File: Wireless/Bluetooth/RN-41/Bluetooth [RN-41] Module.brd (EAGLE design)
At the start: 25.4 x 25.4 mm, 12 parts

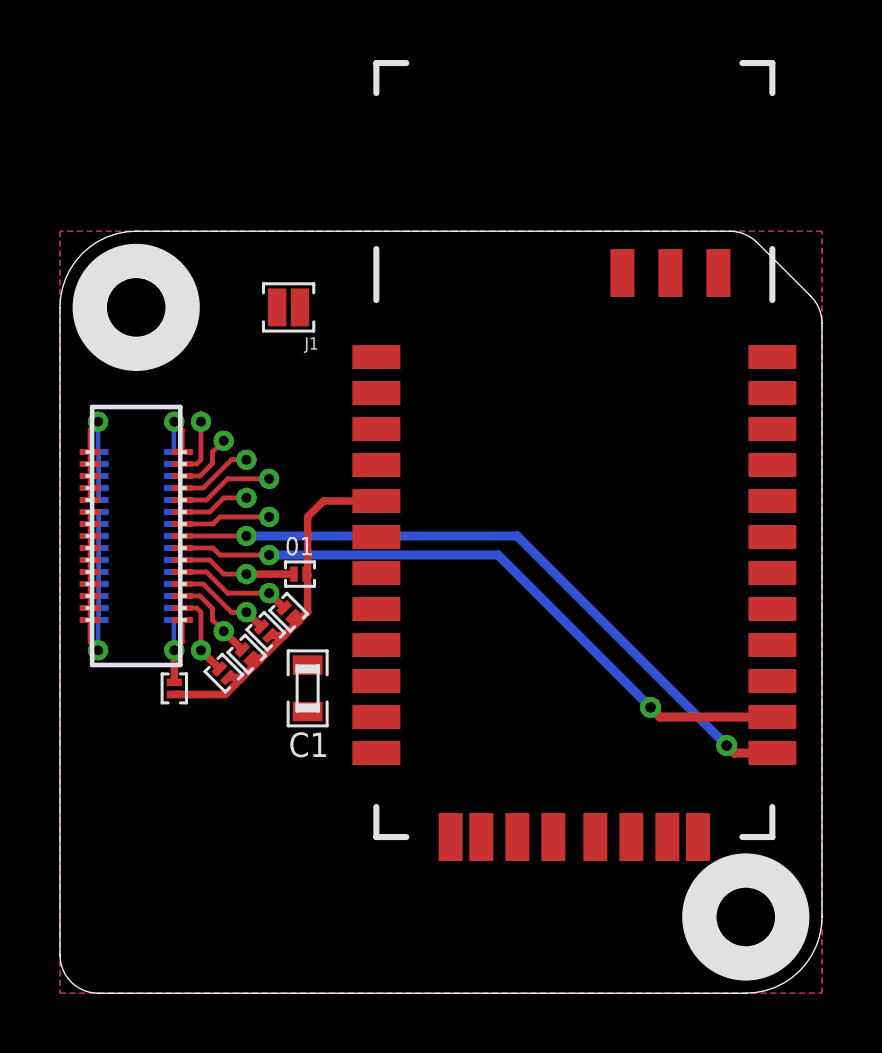
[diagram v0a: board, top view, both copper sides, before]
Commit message: Completed Bluetooth (RN-41) Module
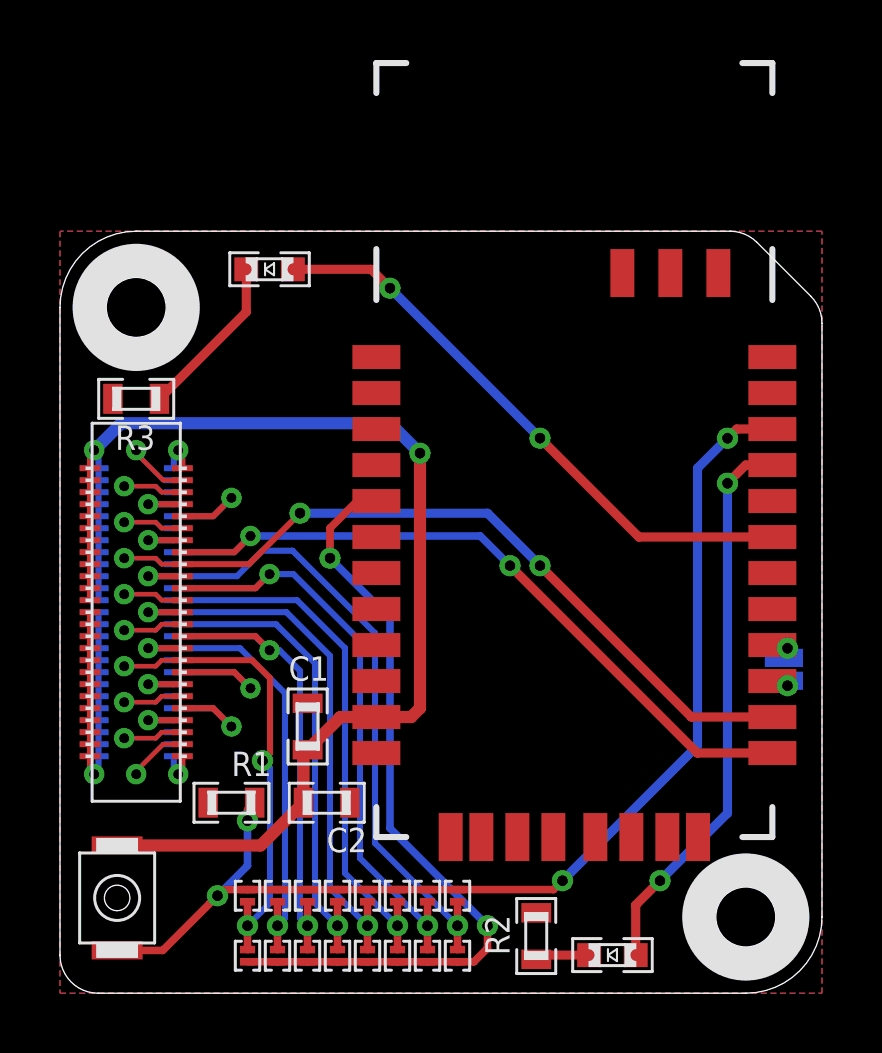
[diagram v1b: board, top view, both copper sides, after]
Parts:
- removed 02, 03: (no value), .solderjumper:2.SML
- added 08, J10, J11, J12, J13, J14, J15, J2, J3, J4, J8, J9: (no value), .solderjumper:2.SML
- added BTN1: SPST.B3U-1000P(M)-B, omron:B3U-1000P(M)-B
- added C2: 1uF, .standardparts:0603
- added LED1, LED2: (no value), .standardparts:0603.LED
- added R1: 100k, .standardparts:0603
- added R2, R3: 1k, .standardparts:0603
- C1: value (none) -> .1uF
- moved J1 20.4 mm to (24.1, 10.8), flipped to the bottom, turned to 270 degrees
- moved J5 11.2 mm to (11.2, 1.25), turned to 270 degrees
- moved 01 10.9 mm to (6.25, 3.25), turned to 90 degrees
- moved J6 10.6 mm to (10.2, 1.25), turned to 270 degrees
- moved J7 10.4 mm to (9.25, 1.25)
- moved C1 1.27 mm to (8.26, 8.89)
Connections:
- new net 01: J2.1, J4.1, U$8.01, U$8.01@1, U$8.01@VIA
- new net 02: J10.1, J3.1, U$8.02, U$8.02@1, U$8.02@VIA
- new net 03: J11.1, J5.1, U$8.03, U$8.03@1, U$8.03@VIA
- new net 04: J12.1, J6.1, U$8.04, U$8.04@1, U$8.04@VIA
- new net 05: J13.1, J7.1, U$8.05, U$8.05@1, U$8.05@VIA
- new net 06: J14.1, J8.1, U$8.06, U$8.06@1, U$8.06@VIA
- new net 07: J15.1, J9.1, U$8.07, U$8.07@1, U$8.07@VIA
- new net N$16: U$8.RXI.DBG, U$8.RXI.DBG@1, U$8.RXI.DBG@VIA
- new net N$17: U$8.TXO.DBG, U$8.TXO.DBG@1, U$8.TXO.DBG@VIA
- new net N$19: U$8.RST, U$8.RST@1, U$8.RST@VIA
- new net N$23: LED1.P$2, R3.1
- new net WAKE: 01.1, 08.1, U$8.WAKE, U$8.WAKE@1, U$8.WAKE@VIA
- net 3.3V: now also BTN1.2, C2.1, U$8.3.3V@11, U$8.3.3V@12, U$8.3.3V@13, U$8.3.3V@14, U$8.3.3V@15, U$8.3.3V@16, U$8.3.3V@17, U$8.3.3V@18, U$8.3.3V@19, U$8.3.3V@20, U$8.3.3V@21, U$8.3.3V@22, U$8.3.3V@23, U$8.3.3V@24
- net AUTO.DISC: now also U$2.20; no longer U$2.22
- net CONNECTED: now also LED1.P$1
- net FACTORY.RST: now also 01.2, BTN1.1, J10.2, J11.2, J12.2, J13.2, J14.2, J15.2, J4.2, R1.1, U$2.22; no longer U$2.20
- net GND: now also C2.2, R1.2, R2.2, R3.2, U$8.GND@21, U$8.GND@22, U$8.GND@23, U$8.GND@24, U$8.GND@25, U$8.GND@26
- net N$10: now also LED2.P$2, R2.1; no longer 01.1, U$8.03, U$8.03@1, U$8.03@VIA
- net N$11: now also U$8.TRST, U$8.TRST@1, U$8.TRST@VIA; no longer 02.1, U$8.04, U$8.04@1, U$8.04@VIA
- net N$12: now also U$8.TMS, U$8.TMS@1, U$8.TMS@VIA; no longer 03.1, U$8.05, U$8.05@1, U$8.05@VIA
- net N$13: now also U$8.TCK, U$8.TCK@1, U$8.TCK@VIA; no longer J5.1, U$8.06, U$8.06@1, U$8.06@VIA
- net N$14: now also U$8.TDO, U$8.TDO@1, U$8.TDO@VIA; no longer J6.1, U$8.07, U$8.07@1, U$8.07@VIA
- net N$15: now also U$8.TDI, U$8.TDI@1, U$8.TDI@VIA; no longer J7.1, U$8.WAKE, U$8.WAKE@1, U$8.WAKE@VIA
- net RST: now also 08.2, J2.2, J3.2, J8.2, J9.2; no longer 01.2, 02.2, 03.2
- net RXI: now also U$8.RXI, U$8.RXI@1, U$8.RXI@VIA; no longer U$8.02, U$8.02@1, U$8.02@VIA
- net STATUS: now also LED2.P$1
- net TXO: now also U$8.TXO, U$8.TXO@1, U$8.TXO@VIA; no longer U$8.01, U$8.01@1, U$8.01@VIA
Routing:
- net FACTORY.RST: track 0.00 -> 38.1 mm, vias 0 -> 4
- net 3.3V: track 0.00 -> 33.1 mm, vias 0 -> 1
- net 01: track 0.00 -> 20.7 mm, vias 0 -> 1
- net CONNECTED: track 0.00 -> 19.7 mm, vias 0 -> 2
- net STATUS: track 0.00 -> 18.7 mm, vias 0 -> 2
- net 03: track 0.00 -> 17.9 mm, vias 0 -> 1
- net 04: track 0.00 -> 16.9 mm, vias 0 -> 1
- net 02: track 0.00 -> 16.0 mm, vias 0 -> 1
- net 05: track 0.00 -> 15.9 mm, vias 0 -> 1
- net 07: track 0.00 -> 13.8 mm, vias 0 -> 1
- net WAKE: track 0.00 -> 13.5 mm, vias 0 -> 2
- net RST: track 12.9 -> 26.3 mm, vias 0 -> 2
- net 06: track 0.00 -> 11.5 mm, vias 0 -> 1
- net N$23: track 0.00 -> 5.52 mm
- net RXI: track 19.0 -> 23.2 mm, vias 1 -> 2
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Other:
- board text added: "CONN"
- board text added: "CTS"
- board text added: "Cruz Monrreal II"
- board text added: "Factory"
- board text added: "InnovativeMaker.com"
- board text added: "RTS"
- board text added: "STAT"
- board text added: "v1"
